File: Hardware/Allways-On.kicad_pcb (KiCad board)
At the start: 2 copper layers, 22.9 x 43.2 mm, 4 parts, among them U1 VS1838B, U2 Arduino_Pro_Micro

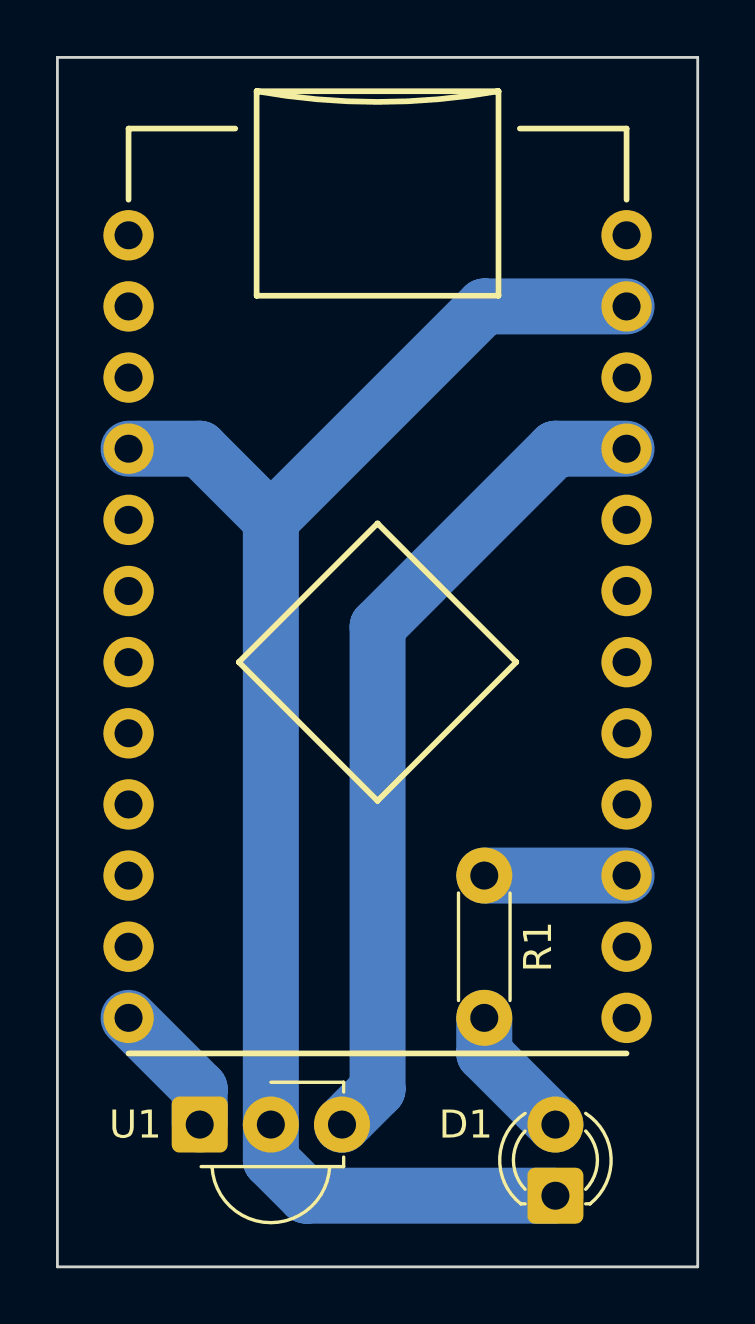
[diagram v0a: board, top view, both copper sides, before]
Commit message: Minor fixes on allways-on PCB
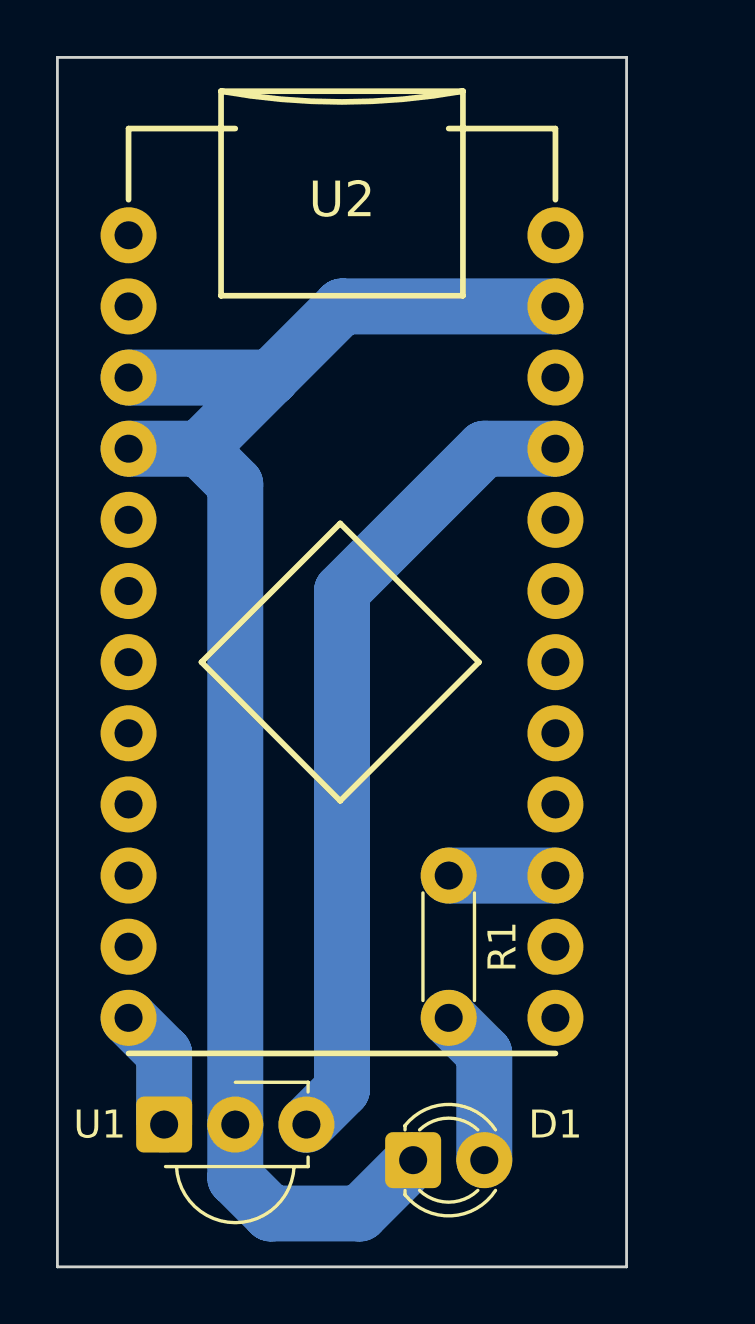
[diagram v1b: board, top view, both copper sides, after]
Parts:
- moved D1 5.24 mm to (152.4, 114.3), turned to 0 degrees
- moved R1 1.27 mm to (153.7, 104.1)
- moved U1 1.27 mm to (143.5, 113.0)
- moved U2 1.27 mm to (149.9, 94.0)
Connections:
- net Net-(D1-K) renamed GND
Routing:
- net Net-(U2-D14): track 5.08 -> 3.81 mm
- net GND: track 55.5 -> 56.7 mm
- net Net-(D1-A): track 4.86 -> 5.61 mm
- net +5V: track 29.8 -> 29.3 mm
- net Net-(U1-OUT): track 4.86 -> 4.34 mm
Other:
- board size 22.9 x 43.2 mm -> 20.3 x 43.2 mm
